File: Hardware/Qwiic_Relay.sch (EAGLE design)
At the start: 34 parts, among them J2 Qwiic Right Angle, J3 Qwiic Right Angle, J4 AVR_SPI_PROG_3X2TESTPOINTS, Q4 600mA/40V, U1 ATTIN85_SOIC_5.3MM, U2 OPTO_ISOLATOR_DIP

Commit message: updated relay to use the sealed version
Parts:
- removed K1: (no value), Relay_SPDT:RELAY_SPDT_1C
- added K2: RELAY-SPDT, SparkFun-Electromechanical:RELAY-SPDT
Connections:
- net COM: now also K2.MAIN; no longer K1.MAIN
- net N$2: now also K2.COIL2; no longer K1.COIL2
- net N$7: now also K2.COIL1; no longer K1.COIL1
- net NC: now also K2.NC; no longer K1.NC
- net NO: now also K2.NO; no longer K1.NO

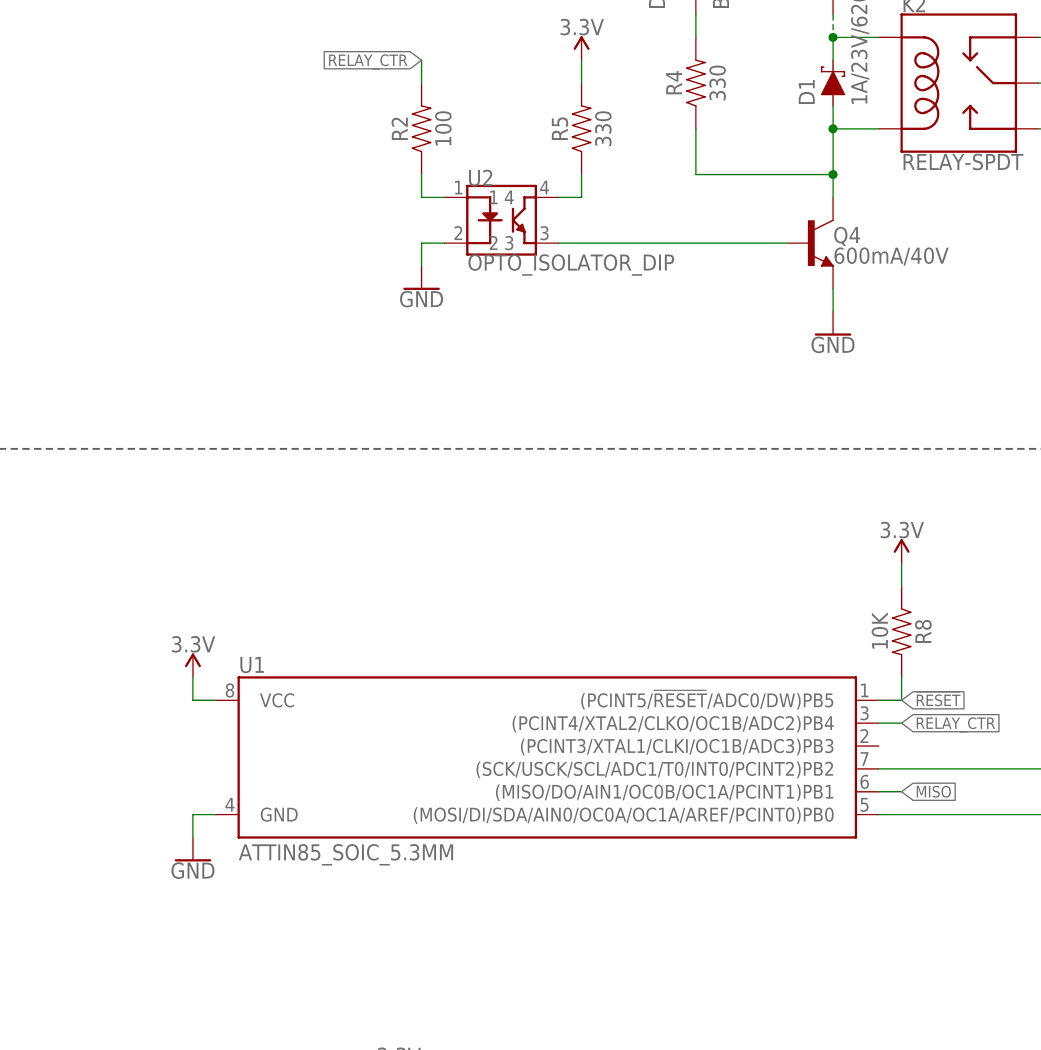
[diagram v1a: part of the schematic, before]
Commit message: updated parts for sparkle parts
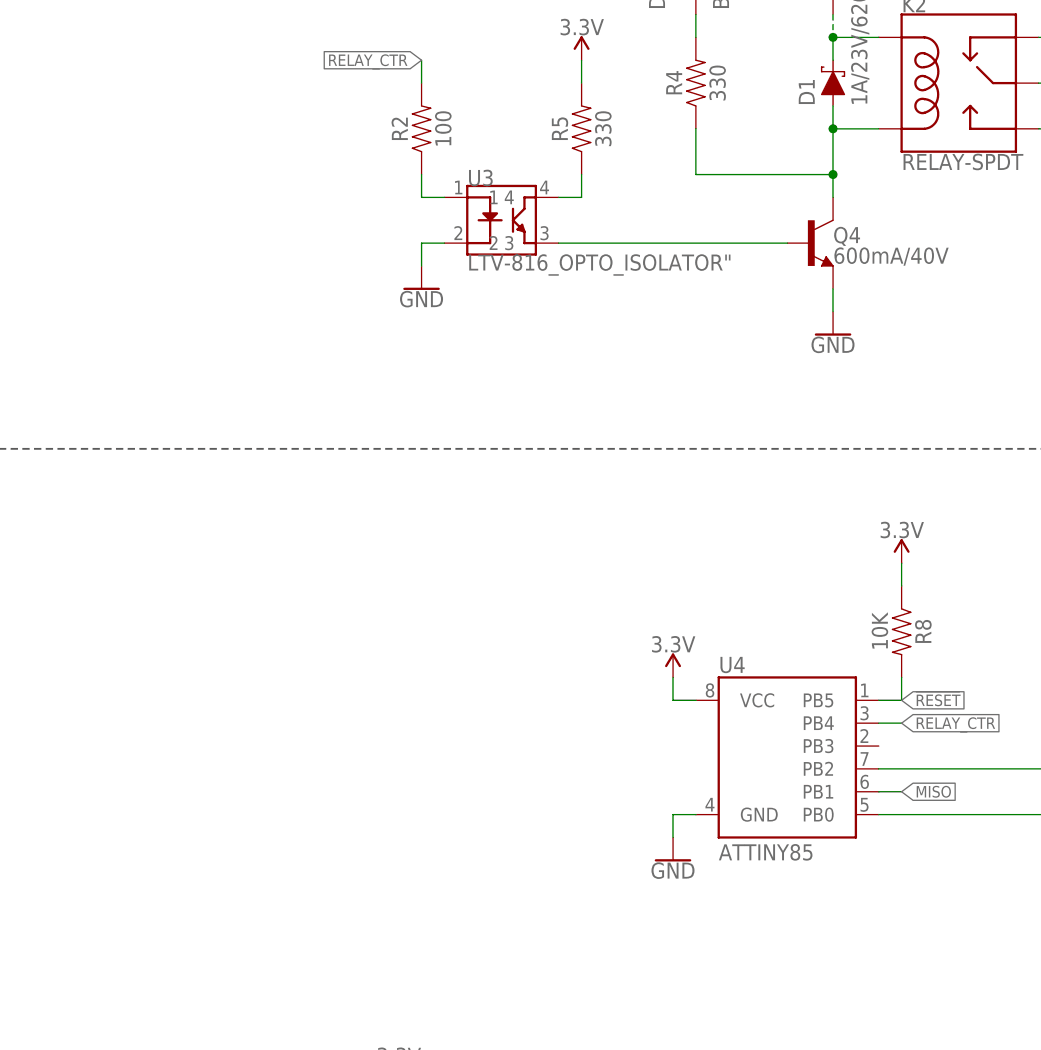
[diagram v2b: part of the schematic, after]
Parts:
- removed U1: ATTIN85_SOIC_5.3MM, attiny85:ATTIN85_SOIC_5.3MM
- removed U2: OPTO_ISOLATOR_DIP, LTV-816:OPTO_ISOLATOR_DIP
- added U3: LTV-816_OPTO_ISOLATOR", SparkFun-DiscreteSemi:LTV-816_OPTO_ISOLATOR"
- added U4: ATTINY85, SparkFun-IC-Microcontroller:ATTINY85
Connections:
- net !RESET: now also U4.PB5; no longer U1.(PCINT5/!RESET!/ADC0/DW)PB5
- net 3.3V: now also U4.VCC; no longer U1.VCC
- net GND: now also U3.2, U4.GND; no longer U1.GND, U2.2
- net MISO: now also U4.PB1; no longer U1.(MISO/DO/AIN1/OC0B/OC1A/PCINT1)PB1
- net N$1: now also U3.3; no longer U2.3
- net N$3: now also U3.1; no longer U2.1
- net N$9: now also U3.4; no longer U2.4
- net RELAY_CTR: now also U4.PB4; no longer U1.(PCINT4/XTAL2/CLKO/OC1B/ADC2)PB4
- net SCL: now also U4.PB2; no longer U1.(SCK/USCK/SCL/ADC1/T0/INT0/PCINT2)PB2
- net SDA: now also U4.PB0; no longer U1.(MOSI/DI/SDA/AIN0/OC0A/OC1A/AREF/PCINT0)PB0
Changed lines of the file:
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@@
 <part name="JP5" library="SparkFun" deviceset="STAND-OFF" device=""/>
 <part name="J5" library="SparkFun-Connectors" deviceset="CONN_03" device="-SCREW-5MM"/>
-<part name="U1" library="attiny85" deviceset="ATTIN85" device="_SOIC_5.3MM"/>
-<part name="U2" library="LTV-816" deviceset="OPTO_ISOLATOR" device="_DIP"/>
 <part name="JP8" library="SparkFun" deviceset="FIDUCIAL" device="UFIDUCIAL"/>
 <part name="JP9" library="SparkFun" deviceset="FIDUCIAL" device="UFIDUCIAL"/>
@@
 <part name="J1" library="SparkFun-Connectors" deviceset="CONN_04" device="1X04_NO_SILK"/>
 <part name="K2" library="SparkFun-Electromechanical" deviceset="RELAY-SPDT" device=""/>
+<part name="U3" library="SparkFun-DiscreteSemi" deviceset="LTV-816_OPTO_ISOLATOR" device="&quot;"/>
+<part name="U4" library="SparkFun-IC-Microcontroller" deviceset="ATTINY85" device=""/>
 </parts>
 <sheets>
@@
 <attribute name="VALUE" x="48.26" y="116.586" size="1.778" layer="96" align="top-center"/>
 </instance>
-<instance part="GND3" gate="1" x="22.86" y="53.34">
-<attribute name="VALUE" x="22.86" y="53.086" size="1.778" layer="96" align="top-center"/>
+<instance part="GND3" gate="1" x="76.2" y="53.34">
+<attribute name="VALUE" x="76.2" y="53.086" size="1.778" layer="96" align="top-center"/>
 </instance>
 <instance part="J2" gate="G$1" x="231.14" y="162.56" rot="MR0">
@@
 <attribute name="VALUE" x="66.04" y="145.034" size="1.778" layer="96" align="bottom-center"/>
 </instance>
-<instance part="SUPPLY4" gate="G$1" x="22.86" y="73.66">
-<attribute name="VALUE" x="22.86" y="76.454" size="1.778" layer="96" align="bottom-center"/>
+<instance part="SUPPLY4" gate="G$1" x="76.2" y="73.66">
+<attribute name="VALUE" x="76.2" y="76.454" size="1.778" layer="96" align="bottom-center"/>
 </instance>
 <instance part="SUPPLY5" gate="G$1" x="45.72" y="27.94">
@@
 <attribute name="NAME" x="170.18" y="167.132" size="1.778" layer="95" font="vector" rot="R180"/>
 </instance>
-<instance part="U1" gate="U1" x="53.34" y="71.12">
-<attribute name="VALUE" x="27.94" y="53.34" size="1.778" layer="96" font="vector"/>
-<attribute name="NAME" x="27.94" y="74.168" size="1.778" layer="95" font="vector"/>
-</instance>
-<instance part="U2" gate="U1" x="53.34" y="127">
-<attribute name="NAME" x="53.34" y="128.27" size="1.778" layer="95" font="vector"/>
-<attribute name="VALUE" x="53.34" y="120.65" size="1.778" layer="96" font="vector" align="top-left"/>
-</instance>
 <instance part="JP8" gate="G$1" x="220.98" y="30.48"/>
 <instance part="JP9" gate="G$1" x="226.06" y="30.48"/>
@@
 <attribute name="NAME" x="101.6" y="147.574" size="1.778" layer="95" font="vector"/>
 <attribute name="VALUE" x="101.6" y="130.048" size="1.778" layer="96" font="vector"/>
+</instance>
+<instance part="U3" gate="U1" x="53.34" y="127">
+<attribute name="NAME" x="53.34" y="128.27" size="1.778" layer="95" font="vector"/>
+<attribute name="VALUE" x="53.34" y="120.65" size="1.778" layer="96" font="vector" align="top-left"/>
+</instance>
+<instance part="U4" gate="U1" x="88.9" y="66.04">
+<attribute name="VALUE" x="81.28" y="53.34" size="1.778" layer="96" font="vector"/>
+<attribute name="NAME" x="81.28" y="74.168" size="1.778" layer="95" font="vector"/>
 </instance>
 </instances>
@@
 <segment>
 <pinref part="GND3" gate="1" pin="GND"/>
-<wire x1="25.4" y1="58.42" x2="22.86" y2="58.42" width="0.1524" layer="91"/>
-<wire x1="22.86" y1="58.42" x2="22.86" y2="55.88" width="0.1524" layer="91"/>
-<pinref part="U1" gate="U1" pin="GND"/>
+<wire x1="78.74" y1="58.42" x2="76.2" y2="58.42" width="0.1524" layer="91"/>
+<wire x1="76.2" y1="58.42" x2="76.2" y2="55.88" width="0.1524" layer="91"/>
+<pinref part="U4" gate="U1" pin="GND"/>
 </segment>
 <segment>
@@
 <wire x1="48.26" y1="121.92" x2="48.26" y2="119.38" width="0.1524" layer="91"/>
 <pinref part="GND2" gate="1" pin="GND"/>
-<pinref part="U2" gate="U1" pin="2"/>
+<pinref part="U3" gate="U1" pin="2"/>
 </segment>
 <segment>
@@
 </segment>
 <segment>
-<pinref part="U1" gate="U1" pin="(PCINT4/XTAL2/CLKO/OC1B/ADC2)PB4"/>
 <wire x1="99.06" y1="68.58" x2="101.6" y2="68.58" width="0.1524" layer="91"/>
 <label x="101.6" y="68.58" size="1.27" layer="95" xref="yes"/>
+<pinref part="U4" gate="U1" pin="PB4"/>
 </segment>
 </net>
@@
 </segment>
 <segment>
-<pinref part="U1" gate="U1" pin="(MOSI/DI/SDA/AIN0/OC0A/OC1A/AREF/PCINT0)PB0"/>
 <label x="137.16" y="58.42" size="1.27" layer="95" xref="yes"/>
 <pinref part="R7" gate="G$1" pin="1"/>
 <wire x1="99.06" y1="58.42" x2="137.16" y2="58.42" width="0.1524" layer="91"/>
 <wire x1="137.16" y1="58.42" x2="137.16" y2="71.12" width="0.1524" layer="91"/>
+<pinref part="U4" gate="U1" pin="PB0"/>
 </segment>
 </net>
@@
 </segment>
 <segment>
-<pinref part="U1" gate="U1" pin="(SCK/USCK/SCL/ADC1/T0/INT0/PCINT2)PB2"/>
 <label x="121.92" y="63.5" size="1.27" layer="95" xref="yes"/>
 <wire x1="99.06" y1="63.5" x2="121.92" y2="63.5" width="0.1524" layer="91"/>
 <pinref part="R6" gate="G$1" pin="1"/>
 <wire x1="121.92" y1="71.12" x2="121.92" y2="63.5" width="0.1524" layer="91"/>
+<pinref part="U4" gate="U1" pin="PB2"/>
 </segment>
 </net>
@@
 <wire x1="66.04" y1="129.54" x2="66.04" y2="127" width="0.1524" layer="91"/>
 <wire x1="63.5" y1="127" x2="66.04" y2="127" width="0.1524" layer="91"/>
-<pinref part="U2" gate="U1" pin="4"/>
+<pinref part="U3" gate="U1" pin="4"/>
 </segment>
 </net>
@@
 </segment>
 <segment>
-<wire x1="22.86" y1="73.66" x2="22.86" y2="71.12" width="0.1524" layer="91"/>
-<wire x1="25.4" y1="71.12" x2="22.86" y2="71.12" width="0.1524" layer="91"/>
+<wire x1="76.2" y1="73.66" x2="76.2" y2="71.12" width="0.1524" layer="91"/>
+<wire x1="78.74" y1="71.12" x2="76.2" y2="71.12" width="0.1524" layer="91"/>
 <pinref part="SUPPLY4" gate="G$1" pin="3.3V"/>
-<pinref part="U1" gate="U1" pin="VCC"/>
+<pinref part="U4" gate="U1" pin="VCC"/>
 </segment>
 <segment>
@@
 <pinref part="R8" gate="G$1" pin="2"/>
 <label x="101.6" y="71.12" size="1.27" layer="95" xref="yes"/>
-<pinref part="U1" gate="U1" pin="(PCINT5/!RESET!/ADC0/DW)PB5"/>
 <wire x1="99.06" y1="71.12" x2="101.6" y2="71.12" width="0.1524" layer="91"/>
+<pinref part="U4" gate="U1" pin="PB5"/>
 </segment>
 <segment>
@@
 <wire x1="48.26" y1="129.54" x2="48.26" y2="127" width="0.1524" layer="91"/>
 <wire x1="48.26" y1="127" x2="50.8" y2="127" width="0.1524" layer="91"/>
-<pinref part="U2" gate="U1" pin="1"/>
+<pinref part="U3" gate="U1" pin="1"/>
 </segment>
 </net>
@@
 <pinref part="Q4" gate="G$1" pin="B"/>
 <wire x1="88.9" y1="121.92" x2="63.5" y2="121.92" width="0.1524" layer="91"/>
-<pinref part="U2" gate="U1" pin="3"/>
+<pinref part="U3" gate="U1" pin="3"/>
 </segment>
 </net>
@@
 </segment>
 <segment>
-<pinref part="U1" gate="U1" pin="(MISO/DO/AIN1/OC0B/OC1A/PCINT1)PB1"/>
 <wire x1="99.06" y1="60.96" x2="101.6" y2="60.96" width="0.1524" layer="91"/>
 <label x="101.6" y="60.96" size="1.27" layer="95" xref="yes"/>
-</segment>
-</net>
+<pinref part="U4" gate="U1" pin="PB1"/>
+</segment>
+</net>
